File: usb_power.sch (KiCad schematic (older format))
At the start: 52 parts

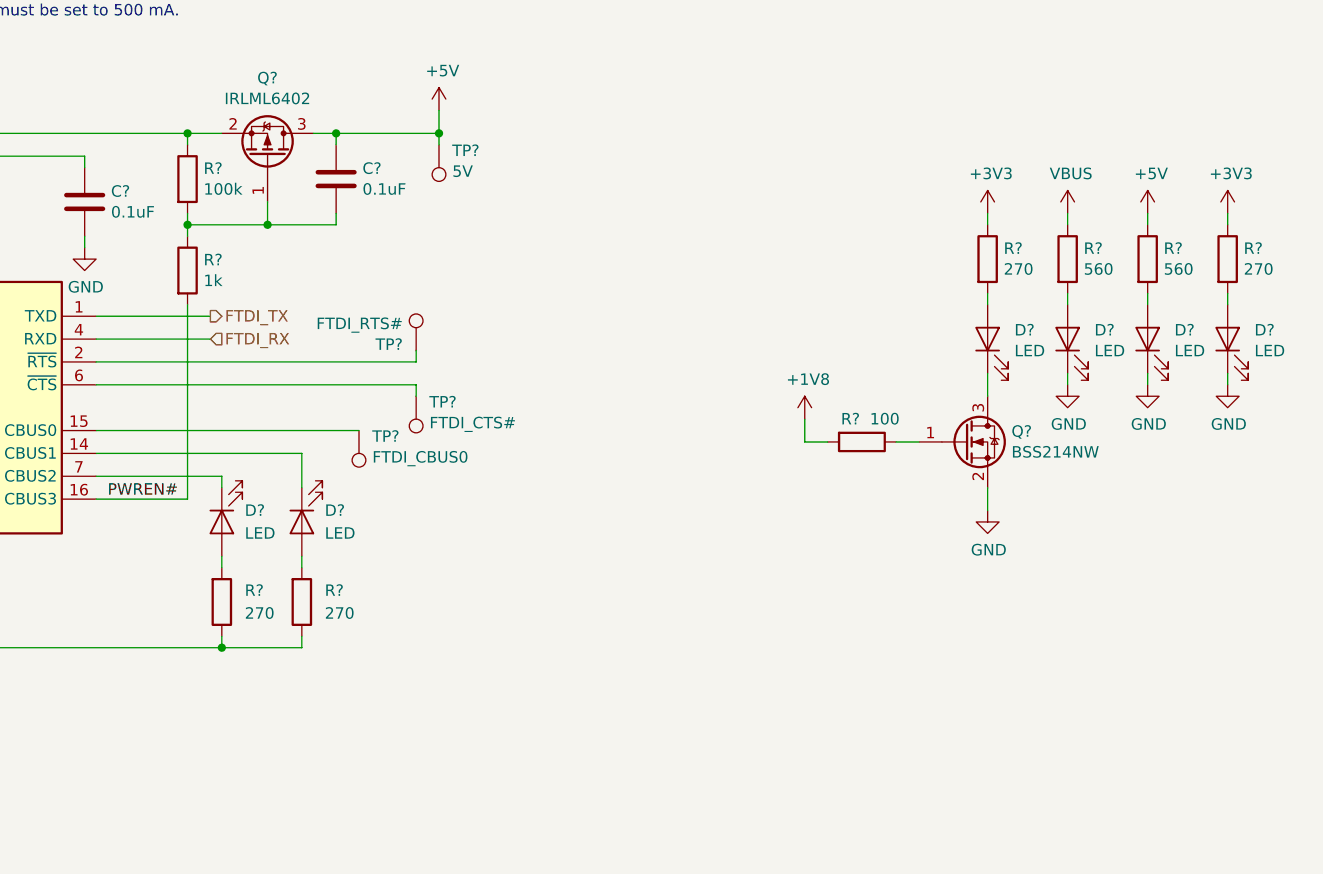
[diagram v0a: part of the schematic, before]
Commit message: Update LEDs descriptions, add main osc footprint
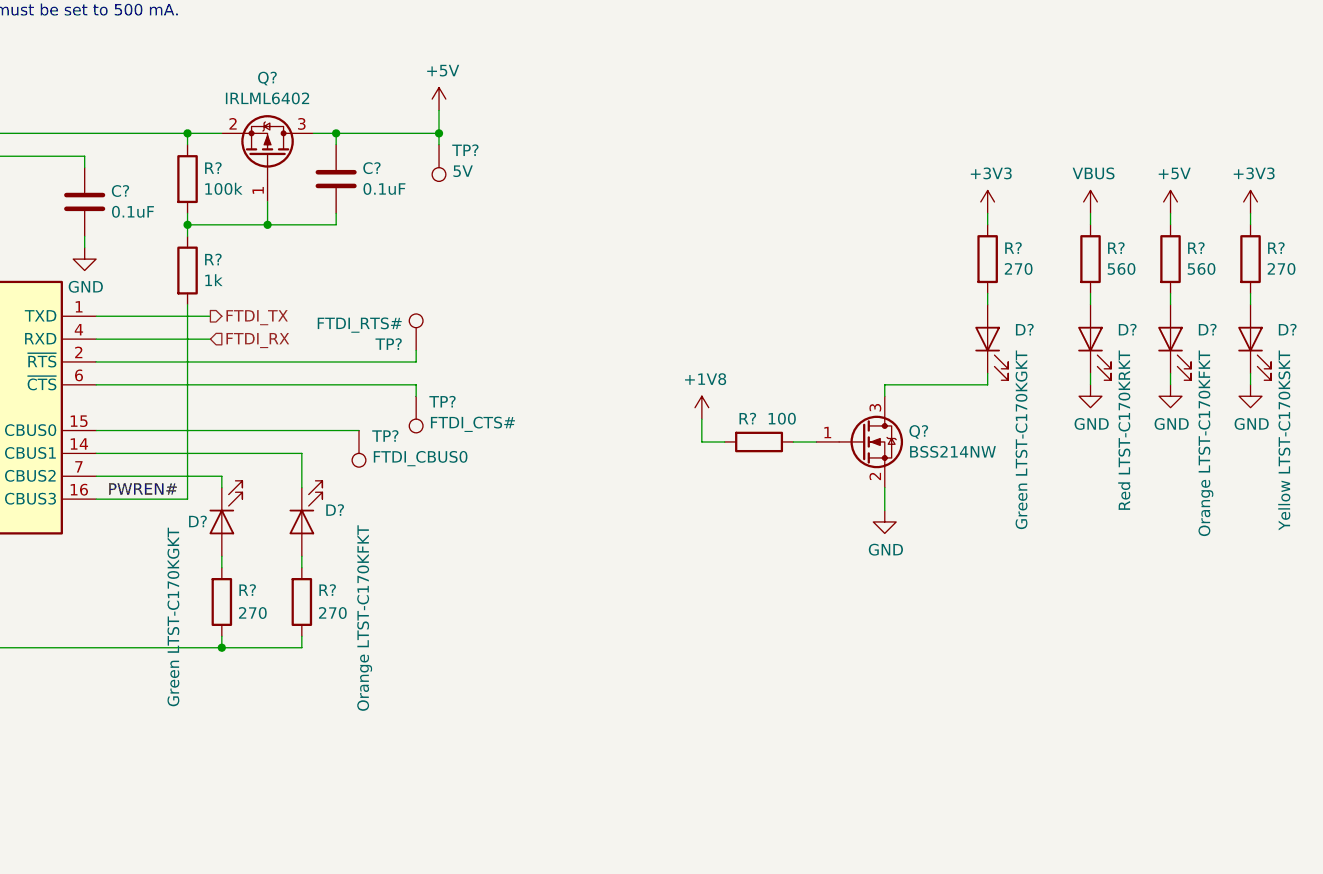
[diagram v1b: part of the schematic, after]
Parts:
- D?: value LED -> Red LTST-C170KRKT
- D? (x2): value LED -> Orange LTST-C170KFKT
- D?: value LED -> Yellow LTST-C170KSKT
- D? (x2): value LED -> Green LTST-C170KGKT
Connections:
- wire segments 172 -> 174
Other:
- moved on the sheet: D?, Q?, R?

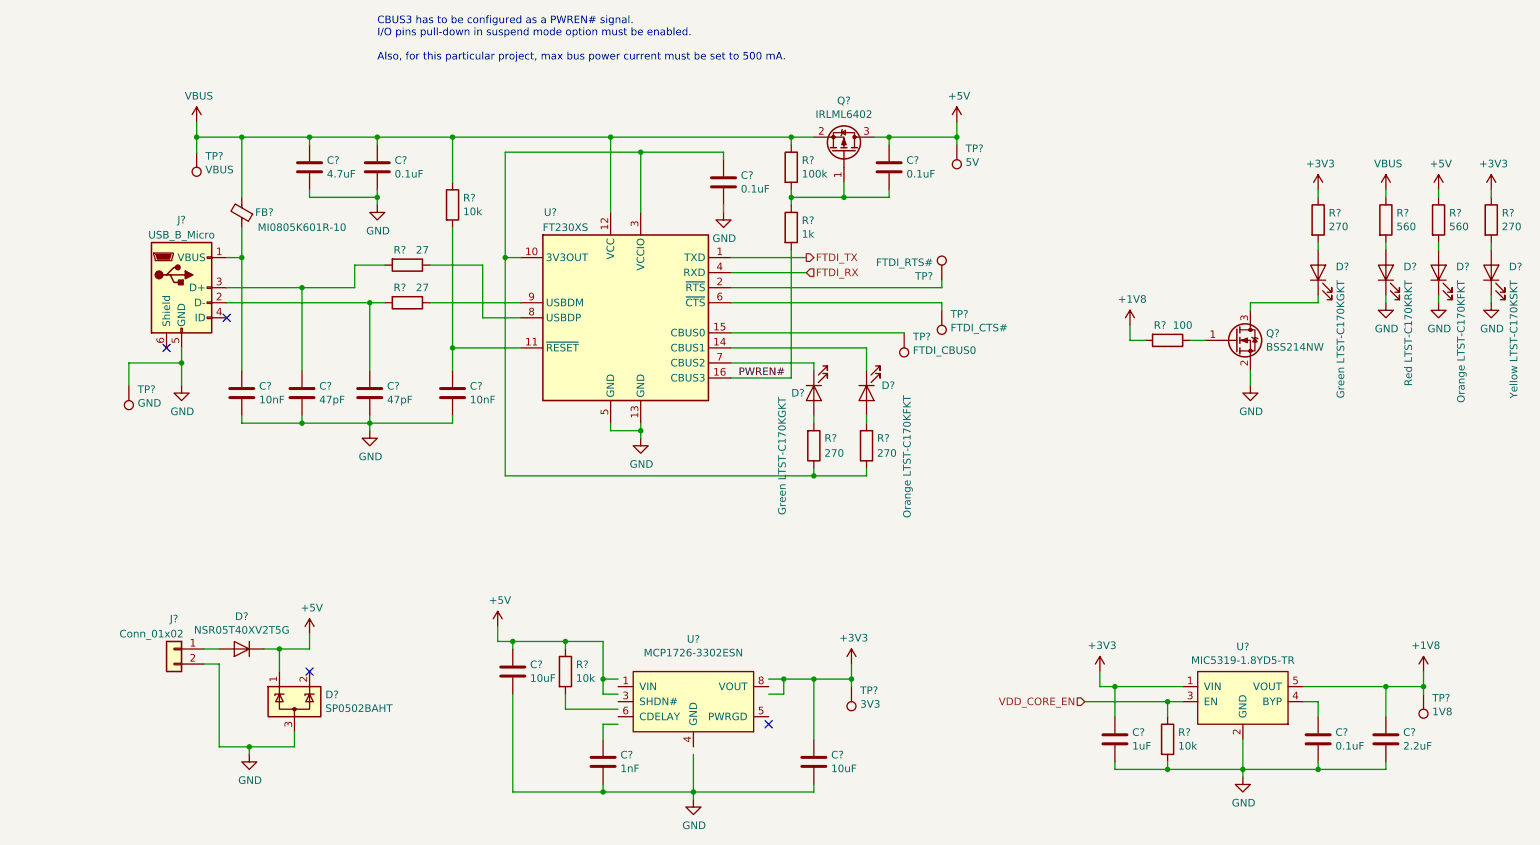
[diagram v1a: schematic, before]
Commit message: First full version of a schematic
This commit is a quicksave of completed but not reviewed schematic.
Added pressure sensor, finished IMU wiring, finished top-level
schematic, added pin header, placed LEDs and many others.
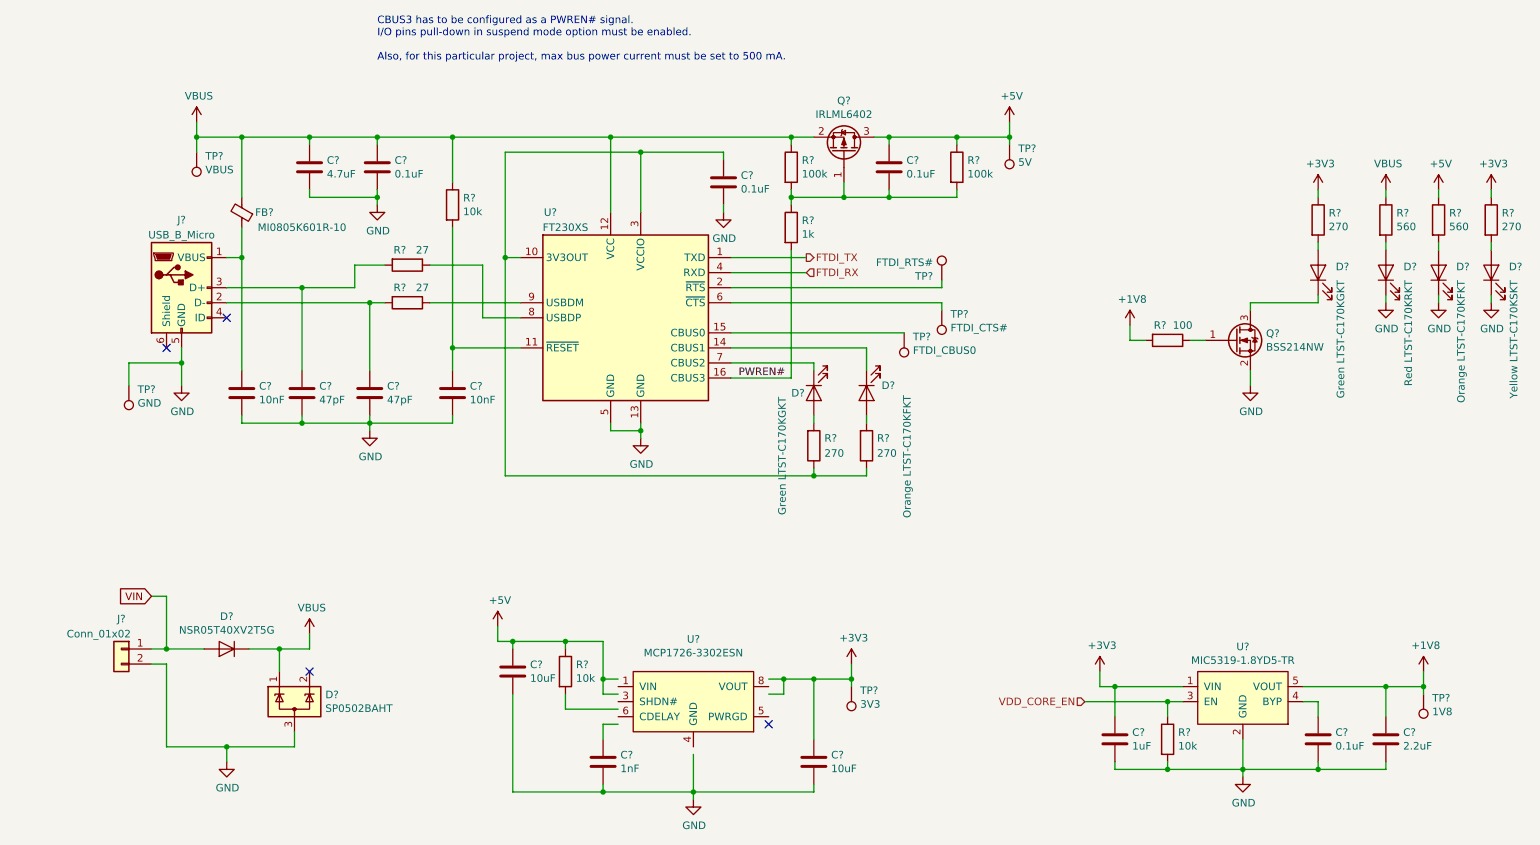
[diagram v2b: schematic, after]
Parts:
- added R?: 100k, symbol Device:R
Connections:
- net labels added: VIN
- wire segments 174 -> 181
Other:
- moved on the sheet: D?, J?, TP?

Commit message: Moved some schematics around, no real changes
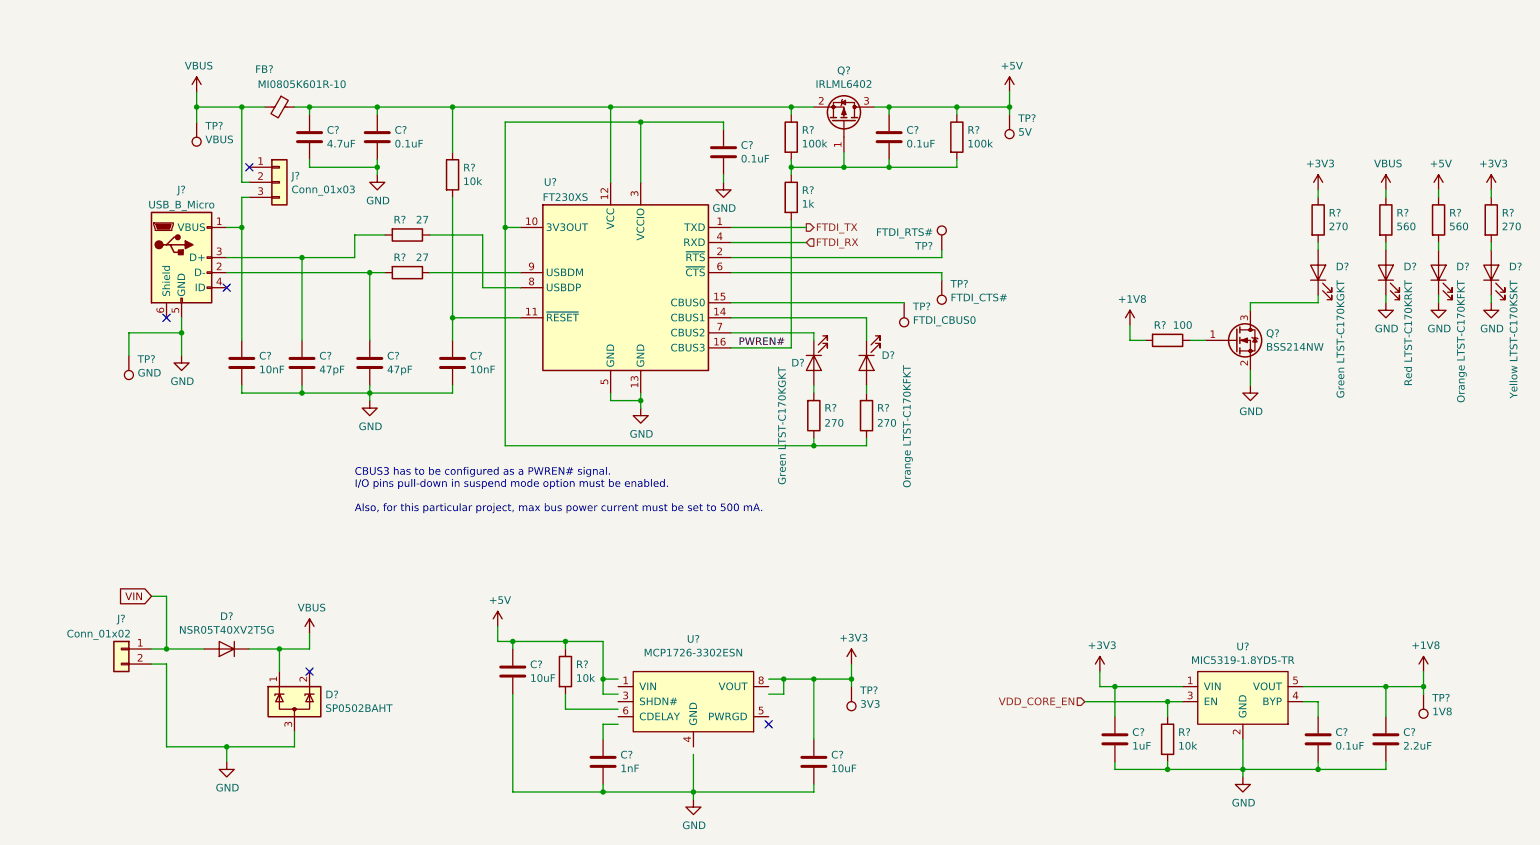
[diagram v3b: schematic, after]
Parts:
- added J?: Conn_01x03, symbol Connector_Generic:Conn_01x03
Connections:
- wire segments 181 -> 184
- no-connect marks 4 -> 5
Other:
- moved on the sheet: C?, D?, FB?, J?, Q?, R?, TP?, U?

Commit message: Add ERC fixes, mostly PWR_FLAGs
Also, fixed MCP1726 symbol.
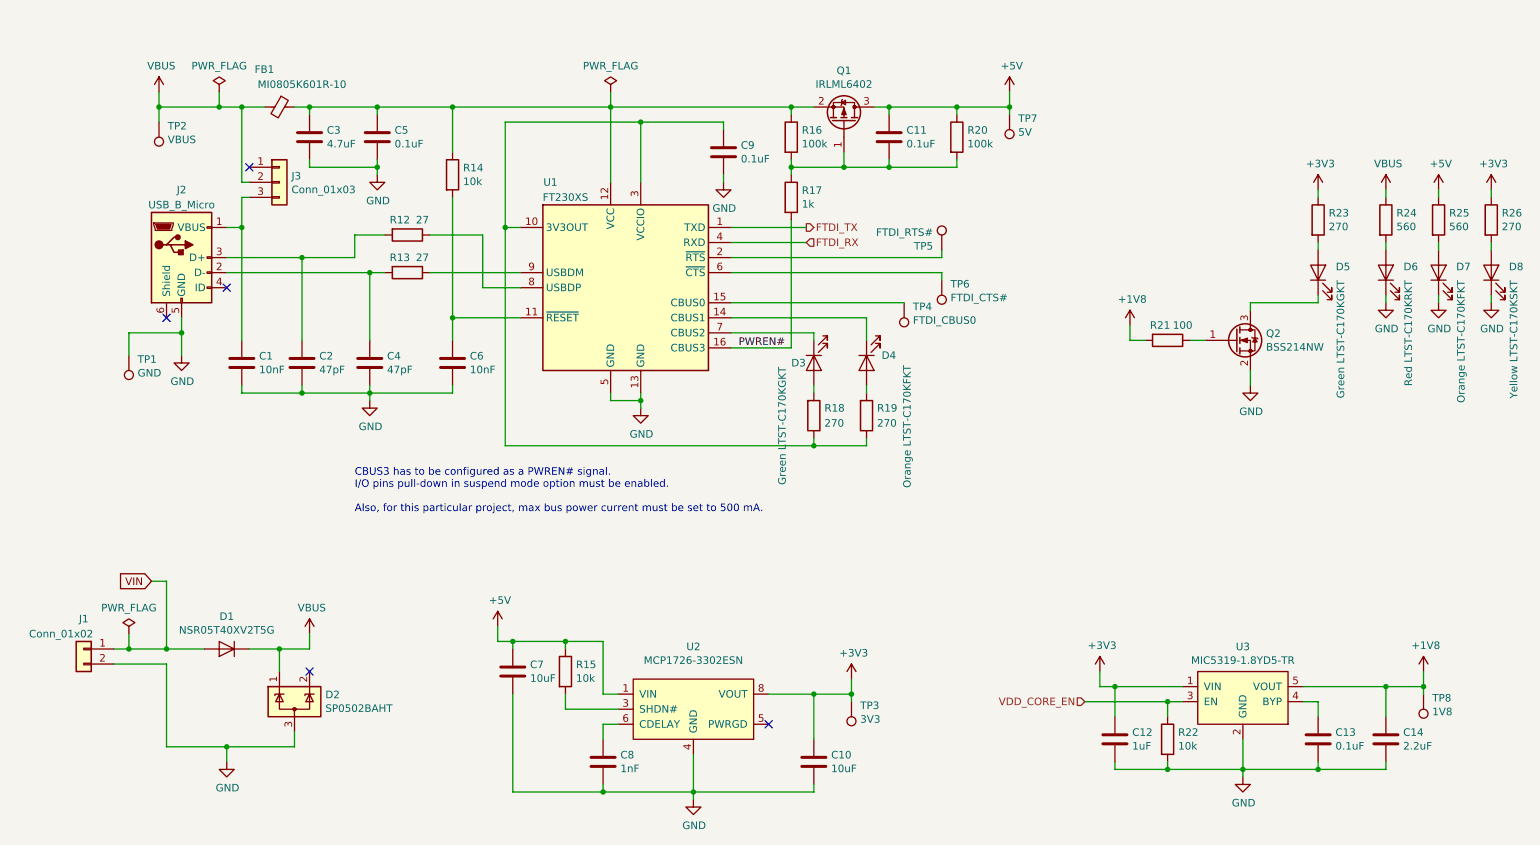
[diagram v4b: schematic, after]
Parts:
- gave numbers to parts that had none: 54
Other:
- moved on the sheet: J1, TP2, TP3, U2

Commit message: Assigned footprints, generated netlist
I can already see some footprints issues. Eg. the switches have to be
changed to the SMT version. There are some silkscreen issues in custom
oscillator footprints. Otherwise looks promising :)
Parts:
- C1, C10, C11, C12, C13, C14, C2, C3, C4, C5, C6, C7, C8, C9: footprint (none) -> Capacitor_SMD:C_0805_2012Metric_Pad1.15x1.40mm_HandSolder
- D1: footprint (none) -> Diode_SMD:D_SOD-523
- D3, D4, D5, D6, D7, D8: footprint (none) -> LED_SMD:LED_0805_2012Metric_Pad1.15x1.40mm_HandSolder
- FB1, R12, R13, R14, R15, R16, R17, R18, R19, R20, R21, R22, R23, R24, R25, R26: footprint (none) -> Resistor_SMD:R_0805_2012Metric_Pad1.15x1.40mm_HandSolder
- J1: footprint (none) -> Connector_PinHeader_2.54mm:PinHeader_1x02_P2.54mm_Vertical_SMD_Pin1Left
- J2: footprint (none) -> Connector_USB:USB_Micro-B_Molex-105017-0001
- J3: footprint (none) -> Connector_PinHeader_2.54mm:PinHeader_1x03_P2.54mm_Vertical_SMD_Pin1Left
- TP1, TP2, TP3, TP4, TP5, TP6, TP7, TP8: footprint (none) -> TestPoint:TestPoint_Pad_D1.5mm
- U3: footprint (none) -> Package_TO_SOT_SMD:TSOT-23-5

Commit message: Reload netlist, set part number of J1 and J3
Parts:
- J1: value Conn_01x02 -> M20-8770642R
- J3: value Conn_01x03 -> M20-8770642R
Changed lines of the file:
@@
 P 900 4950
 F 0 "J1" H 900 5150 50  0000 C CNN
-F 1 "Conn_01x02" H 1050 5050 50  0000 C CNN
+F 1 "M20-8770642R" H 1050 5050 50  0000 C CNN
 F 2 "Connector_PinHeader_2.54mm:PinHeader_1x02_P2.54mm_Vertical_SMD_Pin1Left" H 900 4950 50  0001 C CNN
 F 3 "~" H 900 4950 50  0001 C CNN
@@
 P 2200 1850
 F 0 "J3" H 2280 1892 50  0000 L CNN
-F 1 "Conn_01x03" H 2280 1801 50  0000 L CNN
+F 1 "M20-8770642R" H 2100 1650 50  0000 L CNN
 F 2 "Connector_PinHeader_2.54mm:PinHeader_1x03_P2.54mm_Vertical_SMD_Pin1Left" H 2200 1850 50  0001 C CNN
 F 3 "~" H 2200 1850 50  0001 C CNN
